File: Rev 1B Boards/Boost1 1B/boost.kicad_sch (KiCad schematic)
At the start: 32 parts, among them Q2 BSC059N04LS6, Q3 BSC059N04LS6, U2 LM5123-Q1

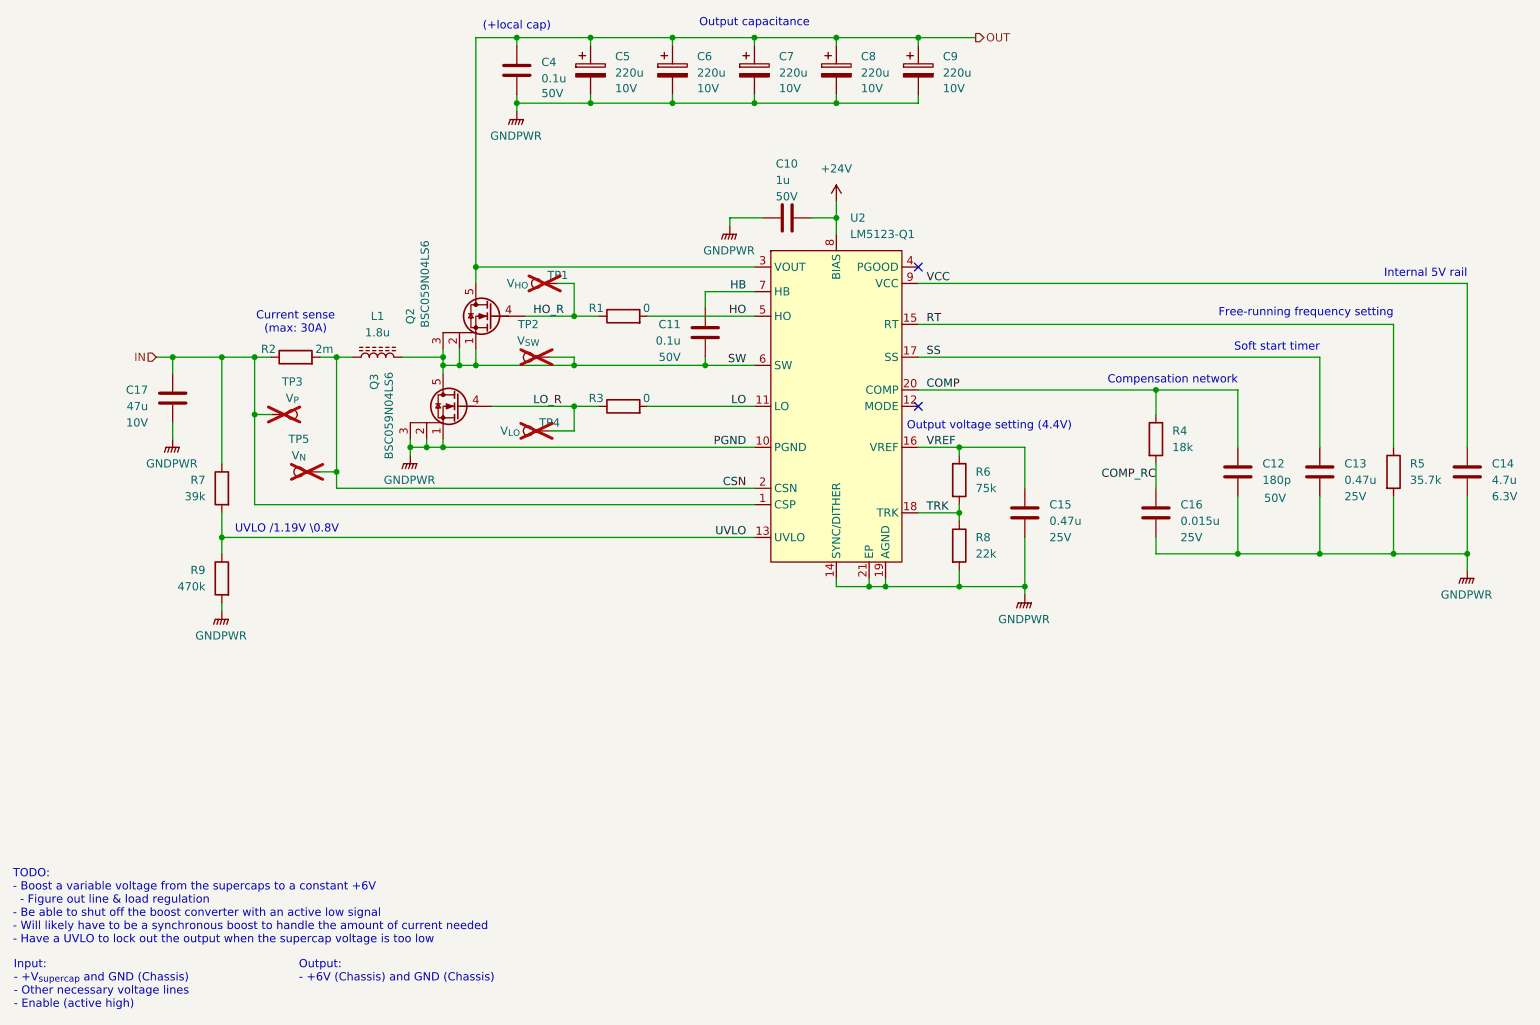
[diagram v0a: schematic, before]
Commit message: Placed footprints for boost stage 1 layout
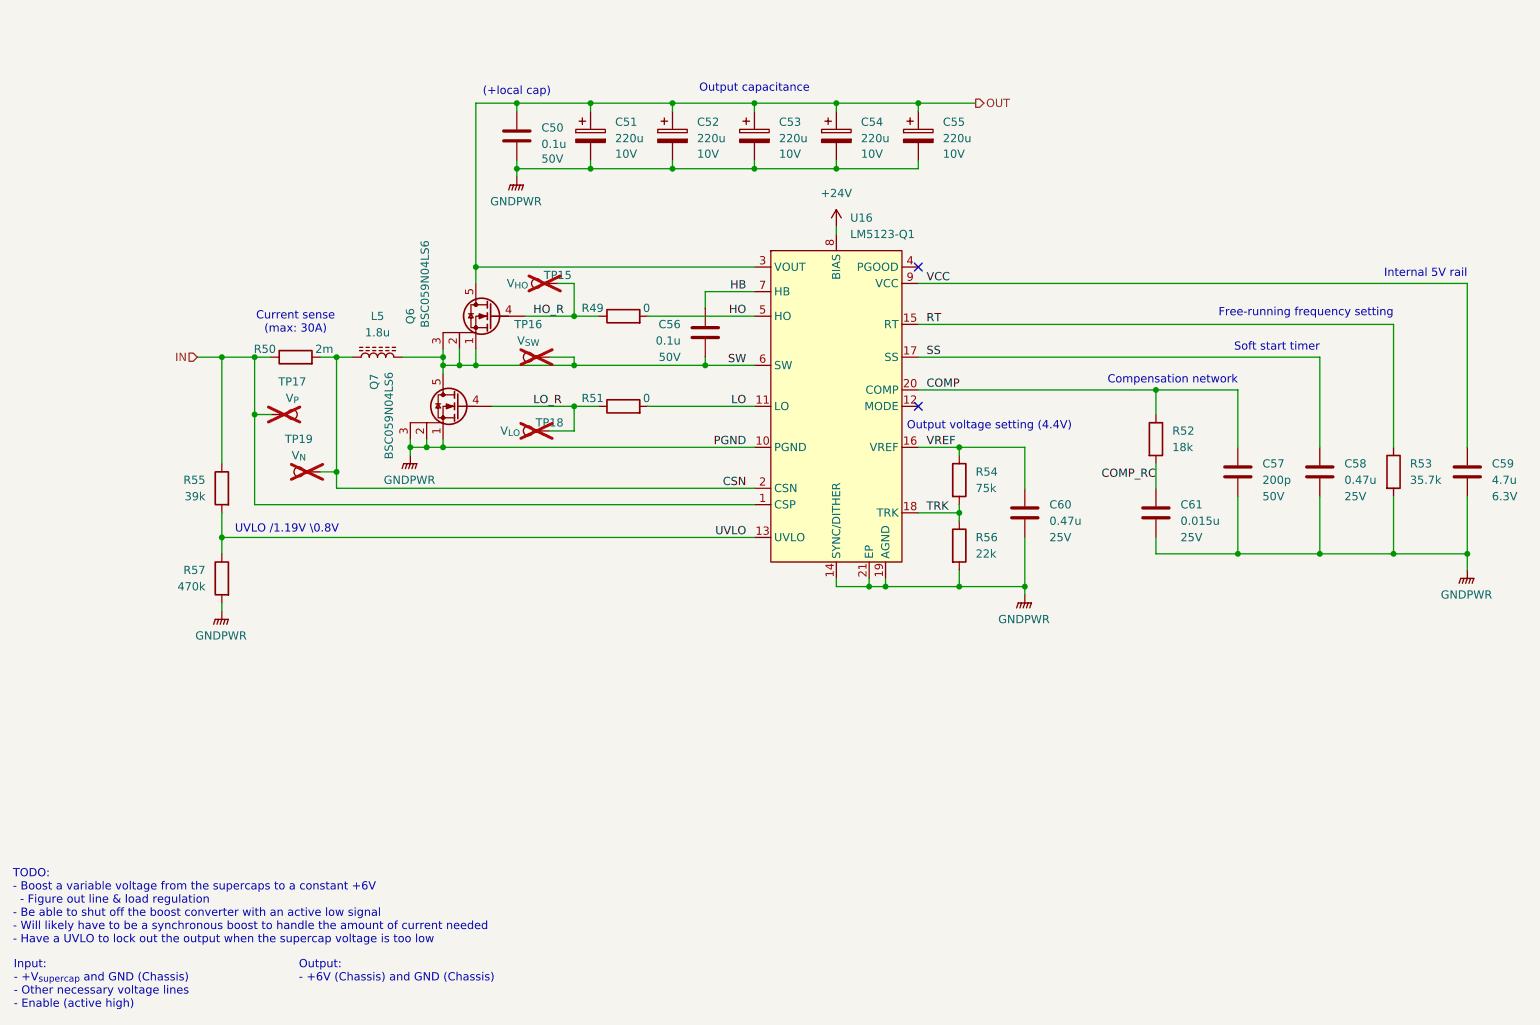
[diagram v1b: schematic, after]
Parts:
- removed C10: 1u, Capacitor_SMD:C_0603_1608Metric_Pad1.08x0.95mm_HandSolder, symbol Device:C
- removed C12: 180p, Capacitor_SMD:C_0603_1608Metric_Pad1.08x0.95mm_HandSolder, symbol Device:C
- removed C17: 47u, Capacitor_SMD:C_1206_3216Metric_Pad1.33x1.80mm_HandSolder, symbol Device:C
- added C57: 200p, Capacitor_SMD:C_0603_1608Metric_Pad1.08x0.95mm_HandSolder, symbol Device:C
- TP15: renamed from TP1; footprint TestPoint:TestPoint_Pad_1.0x1.0mm -> TestPoint:TestPoint_Bridge_Pitch2.0mm_Drill0.7mm
- TP16: renamed from TP2; footprint TestPoint:TestPoint_Pad_1.0x1.0mm -> TestPoint:TestPoint_Bridge_Pitch2.0mm_Drill0.7mm
- TP18: renamed from TP4; footprint TestPoint:TestPoint_Pad_1.0x1.0mm -> TestPoint:TestPoint_Bridge_Pitch2.0mm_Drill0.7mm
- renumbered C4 to C50, C5 to C51, C6 to C52, C7 to C53, C8 to C54, C9 to C55, C11 to C56, C13 to C58, C14 to C59, C15 to C60, C16 to C61, L1 to L5, Q2 to Q6, Q3 to Q7, R1 to R49, R2 to R50, R3 to R51, R4 to R52, R5 to R53, R6 to R54, R7 to R55, R8 to R56, R9 to R57, TP3 to TP17, TP5 to TP19, U2 to U16
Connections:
- net COMP: now also C57.1
- net GNDPWR: now also C57.2
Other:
- moved on the sheet: C50, C51, C52, C53, C54, C55
